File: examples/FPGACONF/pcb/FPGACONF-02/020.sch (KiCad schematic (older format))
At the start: 10 parts, among them CN201 CN_20x2_D1.0mm_P2.54mm_TH, CN202 CN_10x2_D1.0mm_P2.54mm_TH, CN203 CN_20x2_D1.0mm_P2.54mm_TH, CN204 CN_02x1_D1.0mm_P2.54mm_TH, U301 SN74CBTLV3257D

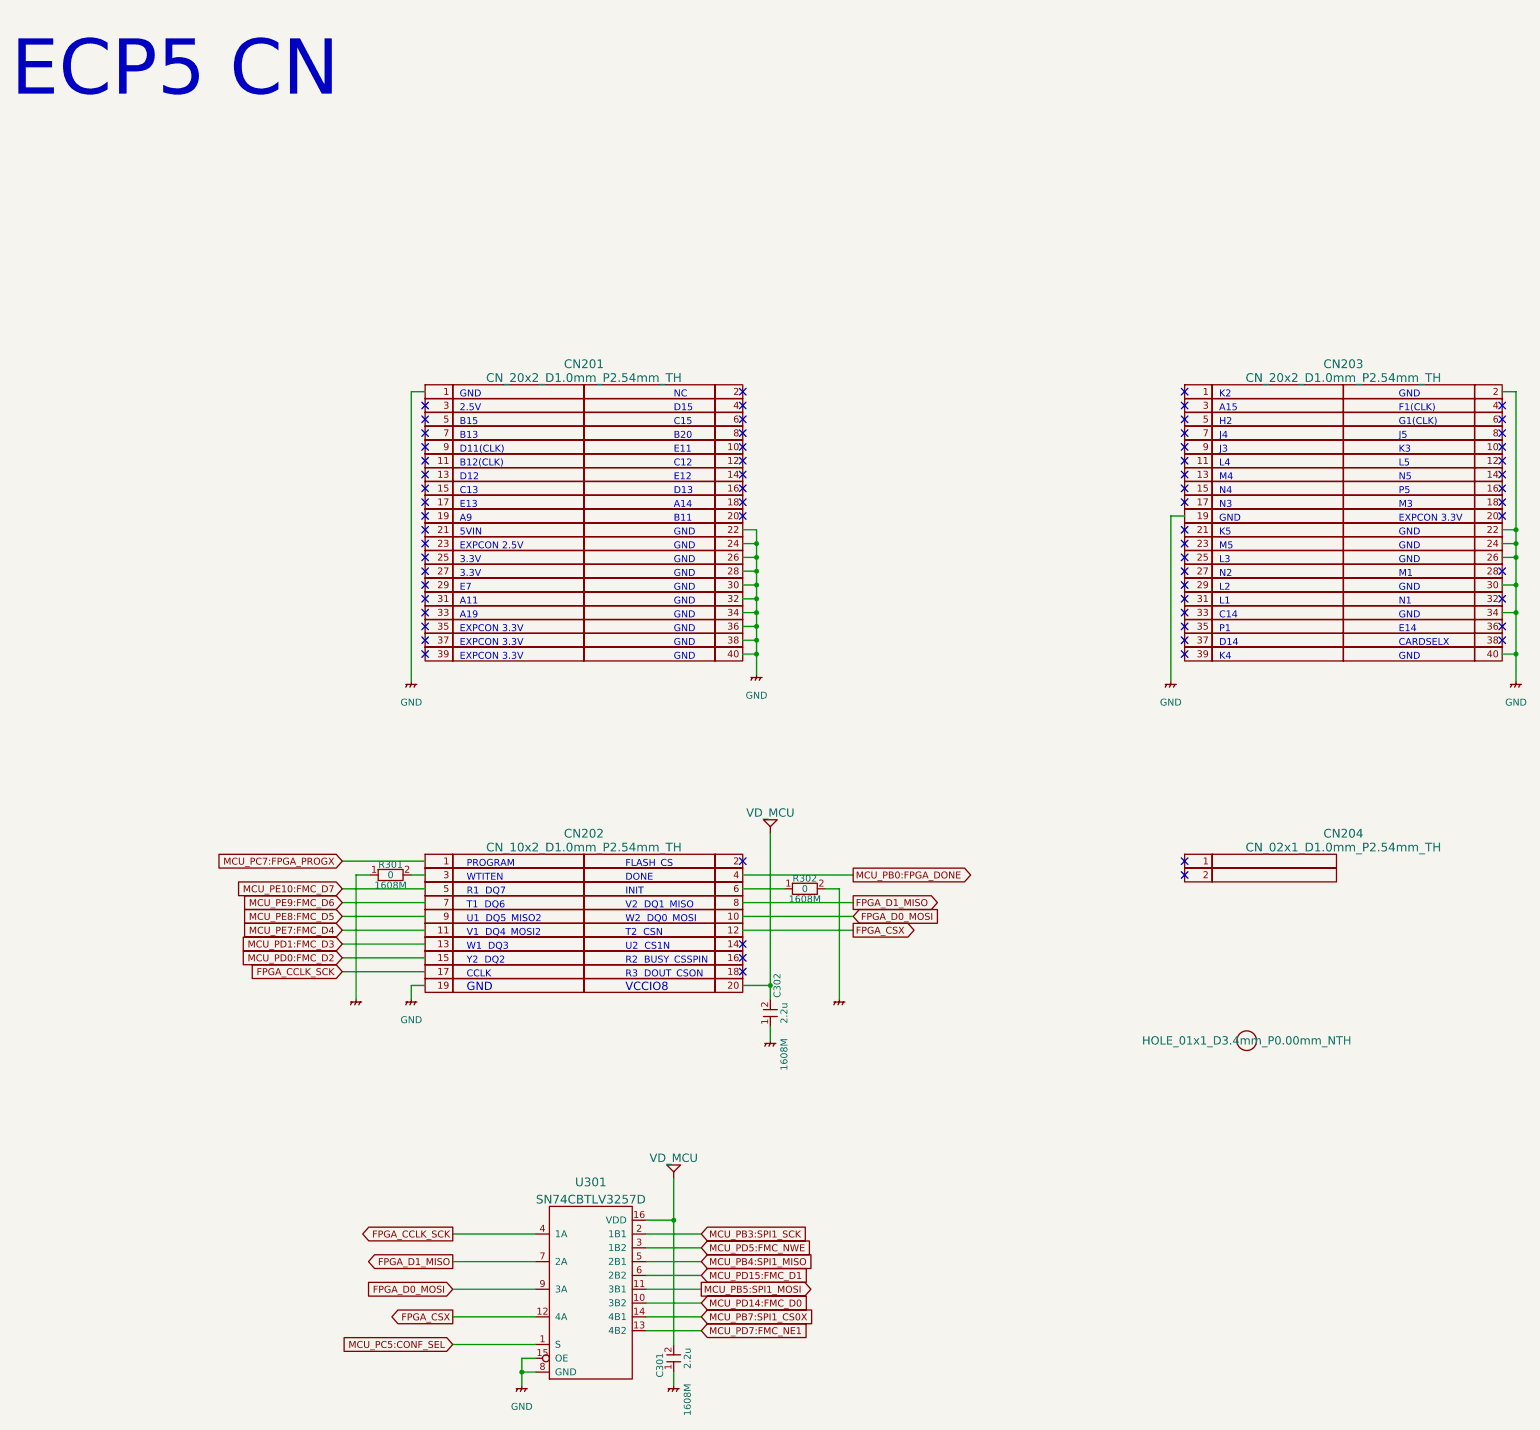
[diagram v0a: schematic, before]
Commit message: FPGACONF-02 schematics  support for SD-DDR (H743) test
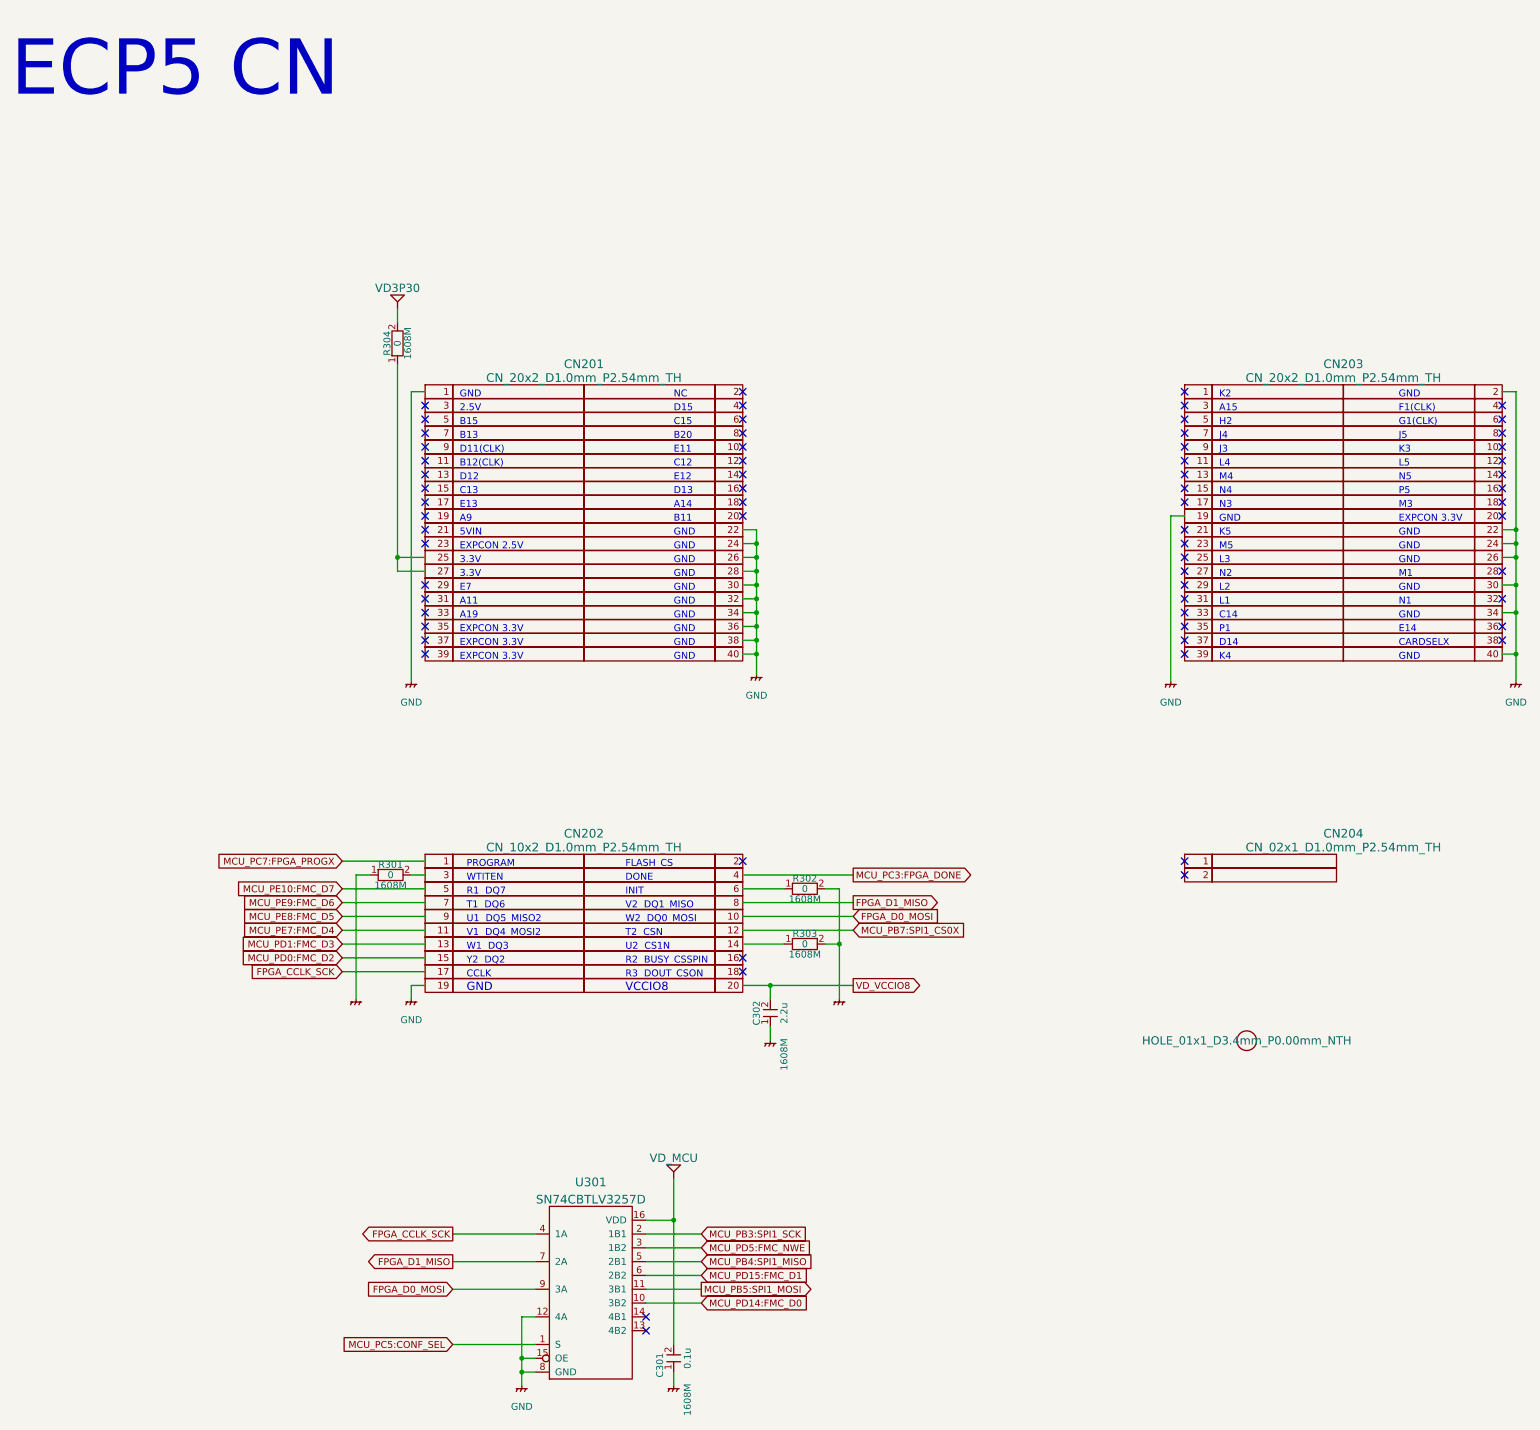
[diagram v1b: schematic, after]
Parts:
- added R303, R304: 0, zhtlab_SMD_standard:RCL_1608m, symbol R-1608M-5%
- C301: value 2.2u -> 0.1u
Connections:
- net MCU_PB7:SPI1_CS0X: now also CN202.12; no longer U301.14 (4B1)
- net VD_MCU: no longer C302.2, CN202.20
- net at CN202.14: now also R303.1
- net at CN201.25: now also CN201.27, R304.1
- net at U301.15 (OE), U301.8 (GND): now also U301.12 (4A)
- net at R302.2: now also R303.2
- removed net FPGA_CSX: CN202.12, U301.12 (4A)
- net MCU_PB0:FPGA_DONE renamed MCU_PC3:FPGA_DONE
- net MCU_PD7:FMC_NE1: no longer names the net of U301.13 (4B2)
- new net VD3P30: R304.2
- new net VD_VCCIO8: C302.2, CN202.20
- no-connect marks 67 -> 66
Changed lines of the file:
@@
 ECP5 CN
 $Comp
-L GND #PWR042
+L GND #PWR043
 U 1 1 5BFE83CB
 P 3600 5400
-F 0 "#PWR042" H 3600 5150 50  0001 C CNN
+F 0 "#PWR043" H 3600 5150 50  0001 C CNN
 F 1 "GND" H 3600 5250 50  0000 C CNN
 F 2 "" H 3600 5400 50  0001 C CNN
@@
 K4
 $Comp
-L GND #PWR043
+L GND #PWR044
 U 1 1 5BFE88BB
 P 6100 5350
-F 0 "#PWR043" H 6100 5100 50  0001 C CNN
+F 0 "#PWR044" H 6100 5100 50  0001 C CNN
 F 1 "GND" H 6100 5200 50  0000 C CNN
 F 2 "" H 6100 5350 50  0001 C CNN
@@
 $EndComp
 $Comp
-L GND #PWR044
+L GND #PWR045
 U 1 1 5BFE89D3
 P 11600 5400
-F 0 "#PWR044" H 11600 5150 50  0001 C CNN
+F 0 "#PWR045" H 11600 5150 50  0001 C CNN
 F 1 "GND" H 11600 5250 50  0000 C CNN
 F 2 "" H 11600 5400 50  0001 C CNN
@@
 Text Notes 5150 7550 0    50   ~ 0
 R3  DOUT_CSON
-Text GLabel 6800 7200 2    50   Output ~ 0
-FPGA_CSX
+Text GLabel 6800 7600 2    50   Output ~ 0
+VD_VCCIO8
 Text Notes 4000 7650 0    60   ~ 0
 GND
@@
 VCCIO8
 $Comp
-L GND #PWR045
+L GND #PWR046
 U 1 1 5BFFDE1C
 P 3600 7700
-F 0 "#PWR045" H 3600 7450 50  0001 C CNN
+F 0 "#PWR046" H 3600 7450 50  0001 C CNN
 F 1 "GND" H 3600 7550 50  0000 C CNN
 F 2 "" H 3600 7700 50  0001 C CNN
@@
 NoConn ~ 6000 3300
 $Comp
-L GND #PWR046
+L GND #PWR047
 U 1 1 5BFFFC74
 P 9100 5400
-F 0 "#PWR046" H 9100 5150 50  0001 C CNN
+F 0 "#PWR047" H 9100 5150 50  0001 C CNN
 F 1 "GND" H 9100 5250 50  0000 C CNN
 F 2 "" H 9100 5400 50  0001 C CNN
@@
 NoConn ~ 3700 3400
 NoConn ~ 3700 4400
-NoConn ~ 3700 4500
-NoConn ~ 3700 4600
 NoConn ~ 3700 5000
 NoConn ~ 3700 5100
@@
 NoConn ~ 6000 7400
 NoConn ~ 6000 7500
-NoConn ~ 6000 7300
 NoConn ~ 11500 4200
 NoConn ~ 3700 4200
@@
 	3100 6700 3700 6700
 Text GLabel 6800 6800 2    50   Output ~ 0
-MCU_PB0:FPGA_DONE
+MCU_PC3:FPGA_DONE
 Wire Wire Line
 	6000 6800 6800 6800
-Text GLabel 5700 10000 2    50   Input ~ 0
-MCU_PB7:SPI1_CS0X
 Text GLabel 5700 9400 2    50   Input ~ 0
 MCU_PB3:SPI1_SCK
@@
 Text GLabel 5700 9500 2    50   Input ~ 0
 MCU_PD5:FMC_NWE
-Text GLabel 5700 10100 2    50   Input ~ 0
-MCU_PD7:FMC_NE1
 Text GLabel 5700 9900 2    50   Input ~ 0
 MCU_PD14:FMC_D0
@@
 Wire Wire Line
 	5700 9900 5300 9900
-Wire Wire Line
-	5300 10000 5700 10000
-Wire Wire Line
-	5700 10100 5300 10100
 Text GLabel 3900 9400 0    50   Output ~ 0
 FPGA_CCLK_SCK
@@
 Text GLabel 3900 9600 0    50   Output ~ 0
 FPGA_D1_MISO
-Text GLabel 3900 10000 0    50   Output ~ 0
-FPGA_CSX
 Wire Wire Line
 	3900 9400 4500 9400
@@
 	3900 9800 4500 9800
 Wire Wire Line
-	4500 10000 3900 10000
-Wire Wire Line
 	4500 10300 4400 10300
 Wire Wire Line
-	4400 10300 4400 10500
+	4400 10000 4400 10500
 Wire Wire Line
 	4500 10400 4400 10400
 Connection ~ 4400 10400
 $Comp
-L GND #PWR047
+L GND #PWR048
 U 1 1 5D80D96D
 P 4400 10500
-F 0 "#PWR047" H 4400 10250 50  0001 C CNN
+F 0 "#PWR048" H 4400 10250 50  0001 C CNN
 F 1 "GND" H 4400 10350 50  0000 C CNN
 F 2 "" H 4400 10500 50  0001 C CNN
@@
 $EndComp
 $Comp
-L GND #PWR048
+L GND #PWR049
 U 1 1 5D8580F0
 P 3200 7700
-F 0 "#PWR048" H 3200 7550 60  0001 C CNN
+F 0 "#PWR049" H 3200 7550 60  0001 C CNN
 F 1 "GND" H 3350 7650 60  0001 C CNN
 F 2 "" H 3200 7700 60  0001 C CNN
@@
 U 1 1 5D8580F8
 P 6200 7800
-F 0 "C302" H 6400 7850 50  0000 C CNN
+F 0 "C302" H 6200 7700 50  0000 C CNN
 F 1 "2.2u" H 6200 7900 50  0000 C CNN
 F 2 "zhtlab_SMD_standard:RCL_1608m" H 6300 7675 79  0001 C CNN
@@
 $EndComp
 Wire Wire Line
-	6200 7600 6000 7600
+	6000 7600 6800 7600
 Connection ~ 6200 7600
-Wire Wire Line
-	6200 7700 6200 6500
-$Comp
-L VD_MCU #PWR049
-U 1 1 5D8581F6
-P 6200 6500
-F 0 "#PWR049" H 6200 6750 60  0001 C CNN
-F 1 "VD_MCU" H 6200 6650 60  0000 C CNN
-F 2 "" H 6200 6600 79  0001 C CNN
-F 3 "" H 6200 6600 79  0001 C CNN
-	1    6200 6500
-	1    0    0    -1
-$EndComp
 $Comp
 L VD_MCU #PWR050
@@
 P 5500 10300
 F 0 "C301" H 5450 10200 50  0000 C CNN
-F 1 "2.2u" H 5500 10400 50  0000 C CNN
+F 1 "0.1u" H 5500 10400 50  0000 C CNN
 F 2 "zhtlab_SMD_standard:RCL_1608m" H 5600 10175 79  0001 C CNN
 F 3 "" H 5400 10300 79  0001 C CNN
@@
 Wire Wire Line
 	6700 6900 6700 7700
+Connection ~ 6700 7300
+Wire Wire Line
+	4500 10000 4400 10000
+Connection ~ 4400 10300
+NoConn ~ 5300 10000
+NoConn ~ 5300 10100
+$Comp
+L R-1608M-5% R303
+U 1 1 5DDF4209
+P 6300 7300
+F 0 "R303" H 6450 7375 50  0000 C CNN
+F 1 "0" H 6450 7300 50  0000 C CNN
+F 2 "zhtlab_SMD_standard:RCL_1608m" H 6100 7100 63  0001 C CNN
+F 3 "" H 6300 7450 79  0001 C CNN
+F 4 "1608M" H 6450 7225 50  0000 C CNN "size"
+F 5 "5%" H 6450 7150 40  0001 C CNN "Tolerance"
+	1    6300 7300
+	1    0    0    -1
+$EndComp
+Wire Wire Line
+	6700 7300 6600 7300
+Wire Wire Line
+	6300 7300 6000 7300
+$Comp
+L VD3P30 #PWR054
+U 1 1 5DE35DCC
+P 3500 2700
+F 0 "#PWR054" H 3500 2950 60  0001 C CNN
+F 1 "VD3P30" H 3500 2850 60  0000 C CNN
+F 2 "" H 3500 2800 79  0001 C CNN
+F 3 "" H 3500 2800 79  0001 C CNN
+	1    3500 2700
+	1    0    0    -1
+$EndComp
+Wire Wire Line
+	3500 3100 3500 4600
+Wire Wire Line
+	3500 4600 3700 4600
+Wire Wire Line
+	3700 4500 3500 4500
+Connection ~ 3500 4500
+$Comp
+L R-1608M-5% R304
+U 1 1 5DE39357
+P 3500 3100
+F 0 "R304" H 3650 3175 50  0000 C CNN
+F 1 "0" H 3650 3100 50  0000 C CNN
+F 2 "zhtlab_SMD_standard:RCL_1608m" H 3300 2900 63  0001 C CNN
+F 3 "" H 3500 3250 79  0001 C CNN
+F 4 "1608M" H 3650 3025 50  0000 C CNN "size"
+F 5 "5%" H 3650 2950 40  0001 C CNN "Tolerance"
+	1    3500 3100
+	0    -1   -1   0
+$EndComp
+Wire Wire Line
+	3500 2700 3500 2800
+Wire Wire Line
+	6200 7700 6200 7600
+Text GLabel 6800 7200 2    50   Input ~ 0
+MCU_PB7:SPI1_CS0X
 $EndSCHEMATC
